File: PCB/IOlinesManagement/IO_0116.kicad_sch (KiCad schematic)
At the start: 144 parts, among them Q17 BC337, Q18 BC337, Q19 BC337, Q20 BC337, Q21 BC337, Q22 BC337, Q23 BC337, Q24 BC337, Q25 BC337, Q26 BC337, Q27 BC337, Q28 BC337, Q29 BC337, Q30 BC337, Q31 BC337, Q32 BC327, Q33 BC327, Q34 BC327, Q35 BC327, Q36 BC327, Q37 BC327, Q38 BC327, Q39 BC327, Q40 BC327, Q41 BC327, Q42 BC327, Q43 BC327, Q44 BC327, Q45 BC327, Q46 BC327, Q7 BC327, Q8 BC337

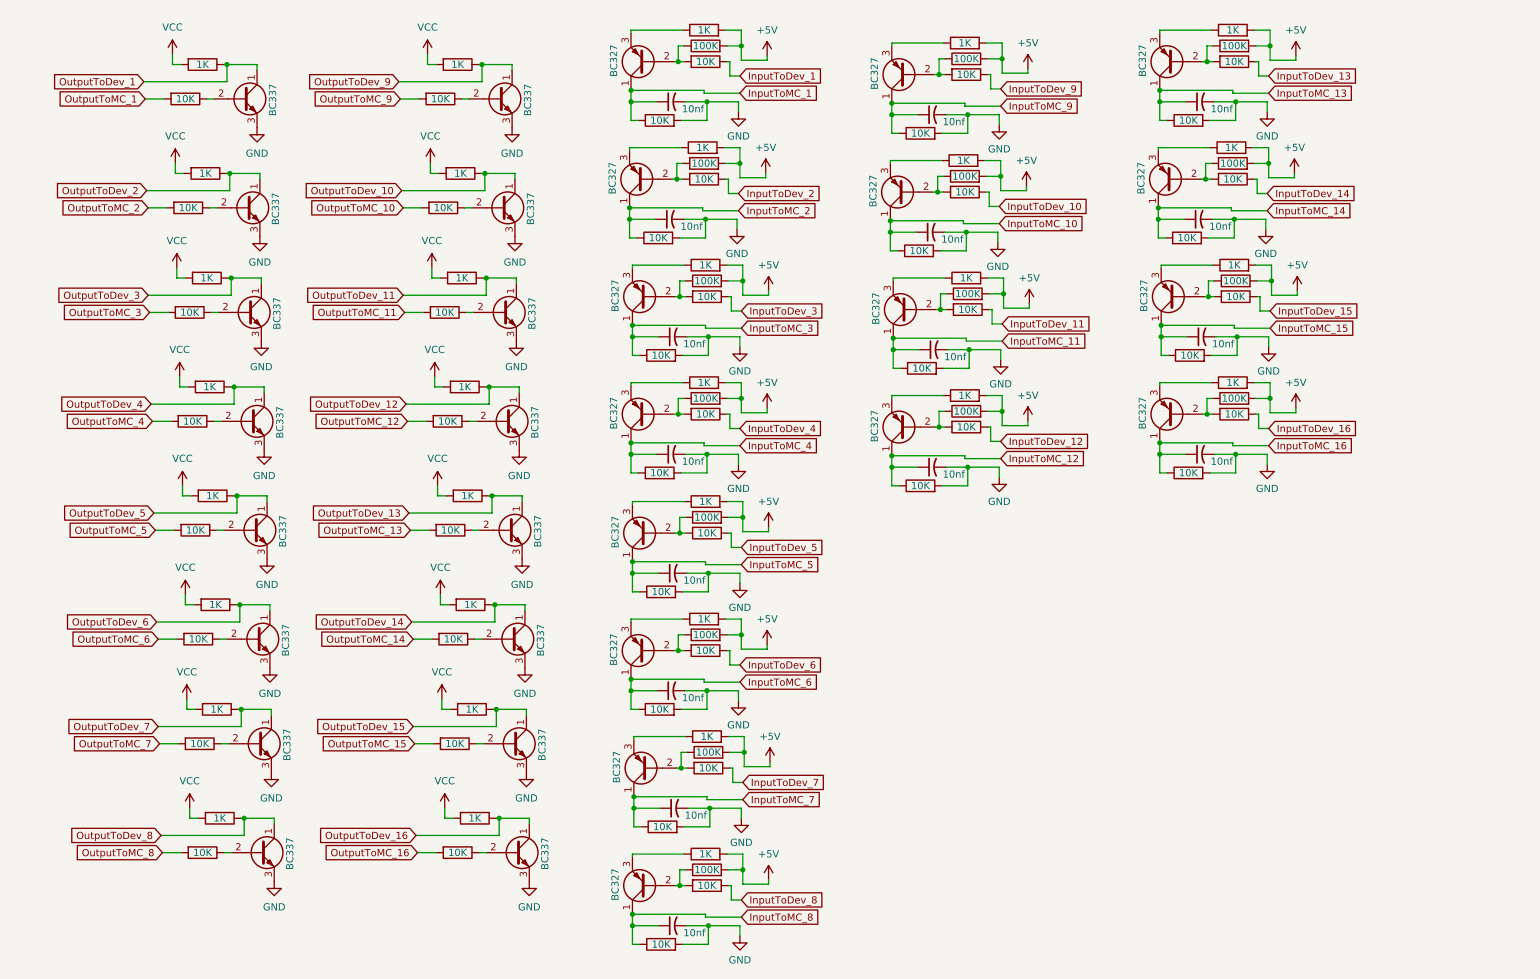
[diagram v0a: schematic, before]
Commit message: Change: push-pull output configuration
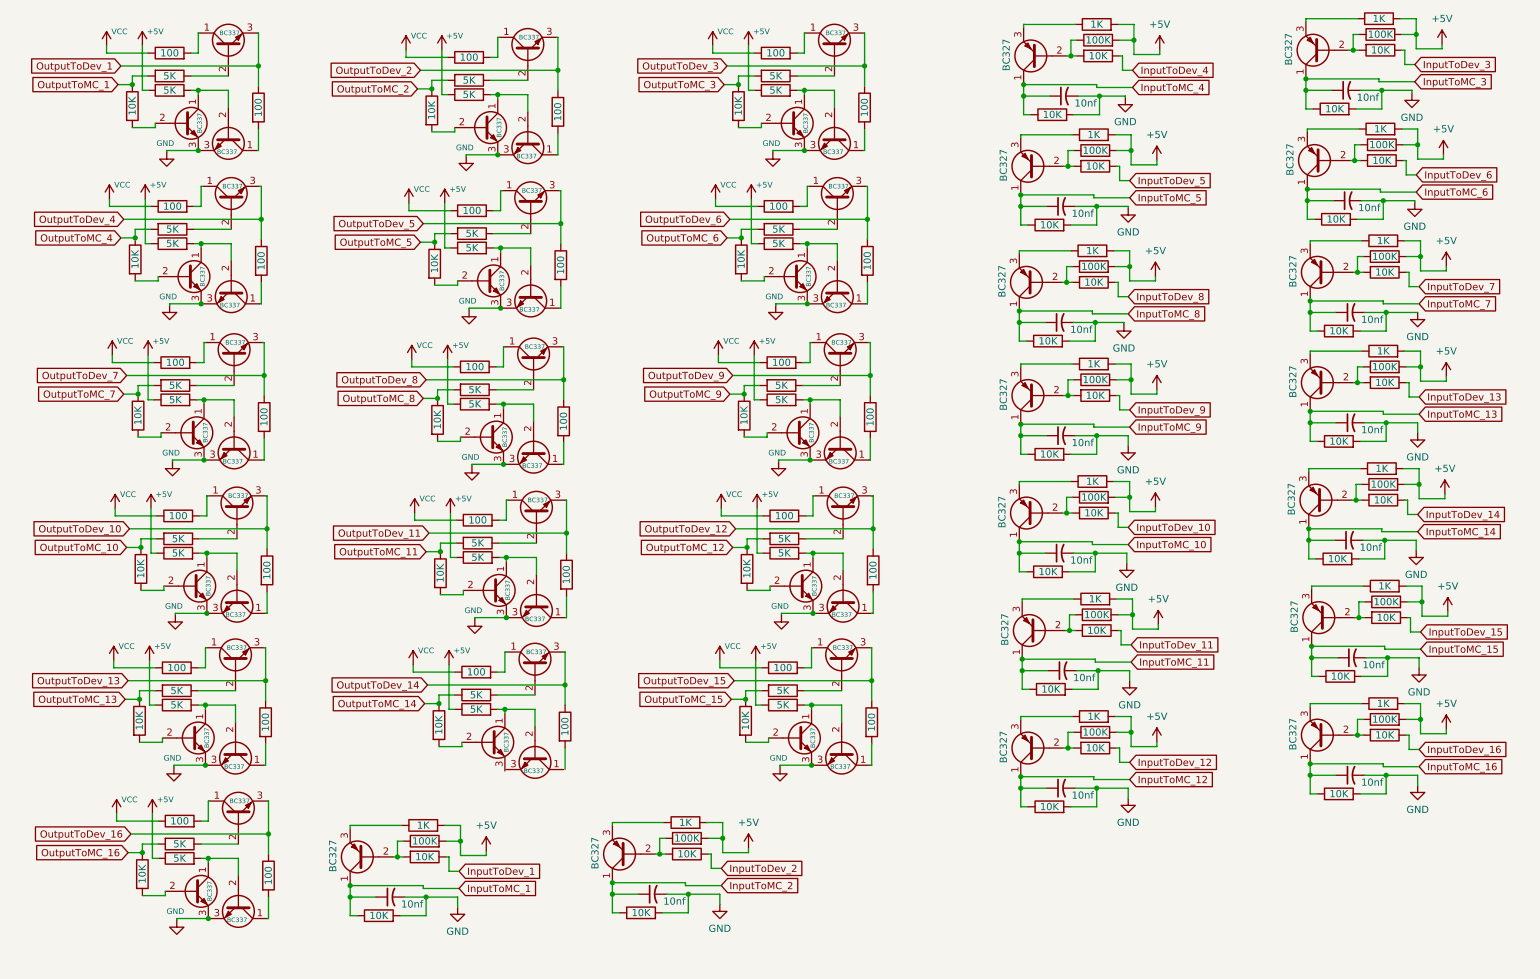
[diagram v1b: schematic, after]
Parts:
- removed Q17, Q18, Q19, Q20, Q21, Q22, Q23, Q24, Q25, Q26, Q27, Q28, Q29, Q30, Q31: BC337, Package_TO_SOT_THT:TO-92_Inline, symbol Transistor_BJT:BC337
- removed R19, R21, R22, R25, R28, R29, R30, R35, R36, R37, R38, R39, R40, R41, R43: 10K, symbol Device:R
- removed R20, R23, R24, R3, R31, R32, R33, R34, R42, R44, R45, R46, R47, R48, R49, R50: 1K, symbol Device:R
- added Q100, Q47, Q48, Q52, Q53, Q54, Q55, Q56, Q57, Q58, Q59, Q60, Q61, Q62, Q63, Q64, Q65, Q66, Q67, Q68, Q69, Q70, Q71, Q72, Q73, Q74, Q75, Q76, Q77, Q78, Q79, Q80, Q81, Q82, Q83, Q84, Q85, Q86, Q87, Q88, Q89, Q90, Q91, Q93, Q94, Q97, Q99: BC337, Package_TO_SOT_THT:TO-92_Inline, symbol Transistor_BJT:BC337
- added R110, R112, R121, R122, R126, R127, R131, R132, R136, R137, R141, R142, R147, R148, R150, R151, R157, R158, R160, R161, R167, R168, R170, R171, R177, R178, R180, R181, R187, R188, R197, R198: 5K, symbol Device:R
- added R111, R113, R120, R123, R125, R128, R130, R133, R135, R138, R140, R143, R146, R149, R152, R153, R156, R159, R162, R163, R166, R169, R172, R173, R176, R179, R182, R183, R186, R192, R196, R202: 100, symbol Device:R
- added R119, R124, R129, R134, R139, R144, R145, R154, R155, R164, R165, R174, R175, R184, R194: 10K, symbol Device:R
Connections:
- net +5V: now also R112.1, R122.1, R127.1, R132.1, R137.1, R142.1, R148.1, R151.1, R158.1, R161.1, R168.1, R171.1, R178.1, R181.1, R188.1, R198.1
- net GND: now also Q100.3 (E), Q48.3 (E), Q52.3 (E), Q54.3 (E), Q55.3 (E), Q57.3 (E), Q58.3 (E), Q60.3 (E), Q61.3 (E), Q63.3 (E), Q64.3 (E), Q66.3 (E), Q67.3 (E), Q68.3 (E), Q70.3 (E), Q72.3 (E), Q73.3 (E), Q74.3 (E), Q76.3 (E), Q78.3 (E), Q79.3 (E), Q80.3 (E), Q82.3 (E), Q84.3 (E), Q85.3 (E), Q86.3 (E), Q88.3 (E), Q90.3 (E), Q97.3 (E)
- net OutputToDev_1: now also Q47.3 (E), R111.1; no longer Q8.1 (C)
- net OutputToDev_10: now also Q71.3 (E), R153.1
- net OutputToDev_11: now also Q77.3 (E), R163.1
- net OutputToDev_12: now also Q83.3 (E), R173.1
- net OutputToDev_13: now also Q87.3 (E), R182.1
- net OutputToDev_14: now also Q93.3 (E), R192.1
- net OutputToDev_15: now also Q99.3 (E), R202.1
- net OutputToDev_16: now also Q89.3 (E), R183.1
- net OutputToDev_2: now also Q53.3 (E), R123.1
- net OutputToDev_3: now also Q56.3 (E), R128.1
- net OutputToDev_4: now also Q59.3 (E), R133.1
- net OutputToDev_5: now also Q62.3 (E), R138.1
- net OutputToDev_6: now also Q65.3 (E), R143.1
- net OutputToDev_7: now also Q69.3 (E), R152.1
- net OutputToDev_8: now also Q75.3 (E), R162.1
- net OutputToDev_9: now also Q81.3 (E), R172.1
- net OutputToMC_1: now also R1.1, R110.2; no longer R1.2
- net OutputToMC_10: now also R145.1, R150.2
- net OutputToMC_11: now also R155.1, R160.2
- net OutputToMC_12: now also R165.1, R170.2
- net OutputToMC_13: now also R174.1, R177.2
- net OutputToMC_14: now also R184.1, R187.2
- net OutputToMC_15: now also R194.1, R197.2
- net OutputToMC_16: now also R175.1, R180.2
- net OutputToMC_2: now also R119.1, R121.2
- net OutputToMC_3: now also R124.1, R126.2
- net OutputToMC_4: now also R129.1, R131.2
- net OutputToMC_5: now also R134.1, R136.2
- net OutputToMC_6: now also R139.1, R141.2
- net OutputToMC_7: now also R144.1, R147.2
- net OutputToMC_8: now also R154.1, R157.2
- net OutputToMC_9: now also R164.1, R167.2
- net VCC: now also R113.1, R120.1, R125.1, R130.1, R135.1, R140.1, R146.1, R149.1, R156.1, R159.1, R166.1, R169.1, R176.1, R179.1, R186.1, R196.1
- net at Q8.2 (B): now also R1.2; no longer R1.1
- new net: Q58.1 (C), Q60.2 (B), R132.2
- new net: Q65.1 (C), R140.2
- new net: Q82.1 (C), R172.2
- new net: Q79.1 (C), Q82.2 (B), R168.2
- new net: Q59.2 (B), R131.1
- new net: Q91.1 (C), Q94.2 (B), R188.2
- new net: Q91.2 (B), R184.2
- new net: Q100.1 (C), R202.2
- new net: Q68.2 (B), R145.2
- new net: Q52.2 (B), R119.2
- new net: Q60.1 (C), R133.2
- new net: Q93.1 (C), R186.2
- new net: Q81.2 (B), R167.1
- new net: Q89.1 (C), R179.2
- new net: Q89.2 (B), R180.1
- new net: Q84.1 (C), R173.2
- new net: Q80.1 (C), Q84.2 (B), R171.2
- new net: Q71.2 (B), R150.1
- new net: Q80.2 (B), R165.2
- new net: Q73.2 (B), R154.2
- new net: Q58.2 (B), R129.2
- new net: Q72.1 (C), R153.2
- new net: Q68.1 (C), Q72.2 (B), R151.2
- new net: Q66.1 (C), R143.2
- new net: Q64.1 (C), Q66.2 (B), R142.2
- new net: Q62.1 (C), R135.2
- new net: Q62.2 (B), R136.1
- new net: Q55.1 (C), Q57.2 (B), R127.2
- new net: Q100.2 (B), Q97.1 (C), R198.2
- new net: Q81.1 (C), R166.2
- new net: Q61.1 (C), Q63.2 (B), R137.2
- new net: Q61.2 (B), R134.2
- new net: Q55.2 (B), R124.2
- new net: Q69.1 (C), R146.2
- new net: Q65.2 (B), R141.1
- new net: Q73.1 (C), Q76.2 (B), R158.2
- new net: Q47.1 (C), R113.2
- new net: Q47.2 (B), R110.1
- new net: Q64.2 (B), R139.2
- new net: Q53.2 (B), R121.1
- new net: Q88.1 (C), R182.2
- new net: Q85.1 (C), Q88.2 (B), R178.2
- new net: Q77.1 (C), R159.2
- new net: Q77.2 (B), R160.1
- new net: Q93.2 (B), R187.1
- new net: Q67.2 (B), R144.2
- new net: Q52.1 (C), Q54.2 (B), R122.2
- new net: Q53.1 (C), R120.2
- new net: Q90.1 (C), R183.2
- new net: Q86.1 (C), Q90.2 (B), R181.2
- new net: Q54.1 (C), R123.2
- new net: Q48.2 (B), Q8.1 (C), R112.2
- new net: Q97.2 (B), R194.2
- new net: Q87.1 (C), R176.2
- new net: Q99.1 (C), R196.2
- new net: Q99.2 (B), R197.1
- new net: Q71.1 (C), R149.2
- new net: Q67.1 (C), Q70.2 (B), R148.2
- new net: Q86.2 (B), R175.2
- new net: Q59.1 (C), R130.2
- new net: Q57.1 (C), R128.2
- new net: Q56.1 (C), R125.2
- new net: Q76.1 (C), R162.2
- new net: Q69.2 (B), R147.1
- new net: Q74.1 (C), Q78.2 (B), R161.2
- new net: Q74.2 (B), R155.2
- new net: Q83.1 (C), R169.2
- new net: Q83.2 (B), R170.1
- new net: Q75.1 (C), R156.2
- new net: Q75.2 (B), R157.1
- new net: Q78.1 (C), R163.2
- new net: Q56.2 (B), R126.1
- new net: Q85.2 (B), R174.2
- new net: Q70.1 (C), R152.2
- new net: Q87.2 (B), R177.1
- new net: Q63.1 (C), R138.2
- new net: Q48.1 (C), R111.2
- new net: Q79.2 (B), R164.2
